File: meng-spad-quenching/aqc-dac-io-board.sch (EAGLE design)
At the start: 13 parts, among them IC5 NC7WZ16P6X, X1 CONN_VREF_CASCODE_IBIAS, X2 CONN_VREF_DIAMOND_IBIAS, X3 CONN_VREF_ONE_SHOT, X4 CONN_PHOTON_COUNTER, X5 CONN_FORCE_QUENCH

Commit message: Added switch cap inverter
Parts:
- added C1, C6, C7: 4u7, rcl:C-EUC0402
- added C14, C16, C27: 2.2u, rcl:C-USC0603
- added C15, C17, C28, C29: 0.1u, rcl:C-USC0603
- added C2, C3, C4, C5: 100n, rcl:C-EUC0402
- added C24: 470n\, rcl:C-USC0603
- added C33: 47u, rcl:C-USC1206
- added IC2: (no value), microbuilder:VREG_SOT23-5
- added IC3: (no value), Kramnik's Library:TPS72301
- added IC4: MAX1680, Kramnik's Library:MAX1680/1
- added LED1: (no value), led:LED3MM
- added R10: 100k, resistor:R-US_R0603
- added R11: 470R, resistor:R-US_R0805
- added R2, R3: 2k2, resistor:R-EU_R0603
- added R21: 64k, resistor:R-US_R0603
- added R22: 36k, resistor:R-US_R0603
- added TP1: TPTP20SQ, testpad:TPTP20SQ
- added X6: USB-MINIB, adafruit:USBMINIB
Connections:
- removed net N$37: IC5.OUT1, IC5.OUT2
- new net +3V3: C14.1, C15.1, IC2.OUT, R10.2
- new net +5V: C16.1, C17.1, C24.1, C33.1, IC2.EN, IC2.IN, R11.1, X6.VBUS
- new net -3V3: C27.1, C28.1, IC3.OUT, R21.1
- new net -5V: C29.1, IC3.EN, IC3.IN
- new net N$11: LED1.A, R11.2
- new net N$14: C7.2, IC4.CAP-
- new net N$15: C7.1, IC4.CAP+
- new net N$19: IC3.FB, R21.2, R22.1
- new net N$2: C3.1, U1.VDD
- new net N$4: IC2.P4, R10.1
- new net N$6: C5.1, U3.VDD
- new net N$7: C4.1, U2.VDD
- new net N$8: R2.2, R3.2
- new net PP_N5V0: C6.1, IC4.OUT
- new net PP_P5V0: ARDUINO_NANO1.5V, C1.1, C2.1, IC4.IN
- net DAC_SCL: now also R2.1
- net DAC_SDA: now also R3.1
- net FORCE_QUENCH_BUF: now also IC5.OUT1, IC5.OUT2
- net GND: now also ARDUINO_NANO1.GND@1, C1.2, C14.2, C15.2, C16.2, C17.2, C2.2, C24.2, C27.2, C28.2, C29.2, C3.2, C33.2, C4.2, C5.2, C6.2, IC2.GND, IC3.GND, IC4.FSEL, IC4.GND, IC4.LV, IC4.SHDN, LED1.C, R22.2, TP1.TP, X6.GND
- net PP_P3V3: now also ARDUINO_NANO1.3V3
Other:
- note added: "+3.3V Linear Regulator"
- note added: "-3.3V Linear Regulator"
- note added: "-5V Switching Converter"
- note added: "Power LED"
- note added: "Scope Ground Clip"
- note added: "USB (Power) Connector"
- note added: "Voltage levels?"
- moved on the sheet: ARDUINO_NANO1, C30, C31, IC5, R1, U1, U2, U3, X1, X2, X3, X4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

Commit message: Started layout, added rescaling opamp and line driver
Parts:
- removed ARDUINO_NANO1: (no value), ArduinoNanoV30:ARDUINO_NANO
- removed C14, C16, C27: 2.2u, rcl:C-USC0603
- removed C15, C17, C28, C29: 0.1u, rcl:C-USC0603
- removed C24: 470n\, rcl:C-USC0603
- removed C33: 47u, rcl:C-USC1206
- removed IC3: (no value), Kramnik's Library:TPS72301
- removed IC5: NC7WZ16P6X, meng:NC7WZ16P6X
- removed LED1: (no value), led:LED3MM
- removed R10: 100k, resistor:R-US_R0603
- removed R11: 470R, resistor:R-US_R0805
- removed R21: 64k, resistor:R-US_R0603
- removed R22: 36k, resistor:R-US_R0603
- removed TP1: TPTP20SQ, testpad:TPTP20SQ
- removed X6: USB-MINIB, adafruit:USBMINIB
- added C8, C9: 100n, rcl:C-EUC0603
- added H1, H2, H3, H4: MOUNT-PAD-ROUND3.2, holes:MOUNT-PAD-ROUND3.2
- added IC1: LT1366, meng:LT1366
- added R4, R7: 10k0, resistor:R-EU_R0603
- added R5: 15k0, resistor:R-EU_R0603
- added R6: 5k11, resistor:R-EU_R0603
- added STM32_NUCLEO: (no value), ArduinoNanoV30:ARDUINO_NANO
- C1, C6, C7: device rcl:C-EUC0402 -> rcl:C-EUC0805
- C2, C3, C30, C31, C4, C5: device rcl:C-EUC0402 -> rcl:C-EUC0603
- IC2: value (none) -> 74LVT126; device microbuilder:VREG_SOT23-5 -> meng:74LVT126
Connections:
- removed net +3V3: C14.1, C15.1, IC2.OUT, R10.2
- removed net +5V: C16.1, C17.1, C24.1, C33.1, IC2.EN, IC2.IN, R11.1, X6.VBUS
- removed net -3V3: C27.1, C28.1, IC3.OUT, R21.1
- removed net -5V: C29.1, IC3.EN, IC3.IN
- removed net LOGIC_QUENCH: IC5.IN1, IC5.IN2
- removed net N$11: LED1.A, R11.2
- removed net N$19: IC3.FB, R21.2, R22.1
- removed net N$4: IC2.P4, R10.1
- new net FORCE_QUENCH_MCU: IC2.1A
- net DAC_SCL: now also STM32_NUCLEO.ADC5/SCL/A5; no longer ARDUINO_NANO1.ADC5/SCL/A5
- net DAC_SDA: now also STM32_NUCLEO.ADC4/SDA/A4; no longer ARDUINO_NANO1.ADC4/SDA/A4
- net FORCE_QUENCH_BUF: now also IC2.1Y; no longer IC5.OUT1, IC5.OUT2
- net GND: now also C8.2, C9.2, H1.MOUNT, H2.MOUNT, H3.MOUNT, H4.MOUNT, IC1B.+IN, IC2.2A, IC2.2OE, IC2.3A, IC2.3OE, IC2.4A, IC2.4OE, R7.1, STM32_NUCLEO.GND@1, STM32_NUCLEO.GND@2; no longer ARDUINO_NANO1.GND@1, ARDUINO_NANO1.GND@2, C14.2, C15.2, C16.2, C17.2, C24.2, C27.2, C28.2, C29.2, C33.2, IC3.GND, IC5.GND, LED1.C, R22.2, TP1.TP, X6.GND
- net N$2: now also R4.2, U1.VOUT; no longer C3.1, U1.VDD
- net N$3: now also IC1B.-IN, R4.1, R5.2; no longer U2.VOUT, X2G1.1
- net N$5: now also IC1B.OUT, R5.1; no longer U1.VOUT
- net N$6: now also IC1A.+IN, U2.VOUT; no longer C5.1, U3.VDD
- net N$7: now also IC1A.OUT, R6.2, X2G1.1; no longer C4.1, U2.VDD
- net N$8: now also IC1A.-IN, R6.1, R7.2; no longer R2.2, R3.2
- net PP_N5V0: now also C8.1, IC1A.V-
- net PP_P3V3: now also C3.1, C4.1, C5.1, IC2.1OE, IC2.VDD, R2.2, R3.2, STM32_NUCLEO.3V3, U1.VDD, U2.VDD, U3.VDD; no longer ARDUINO_NANO1.3V3, IC5.VCC
- net PP_P5V0: now also C9.1, IC1A.V+, STM32_NUCLEO.5V; no longer ARDUINO_NANO1.5V
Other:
- note added: "0V to -5V"
- note added: "0V to 3.3V"
- note added: "0V to 5V"
- note removed: "+3.3V Linear Regulator"
- note removed: "-3.3V Linear Regulator"
- note removed: "-5V Switching Converter"
- note removed: "Power LED"
- note removed: "Scope Ground Clip"
- note removed: "USB (Power) Connector"
- note removed: "Voltage levels?"
- moved on the sheet: C3, C30, C31, C4, C5, R1, R2, R3, U1, U2, U3, X1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

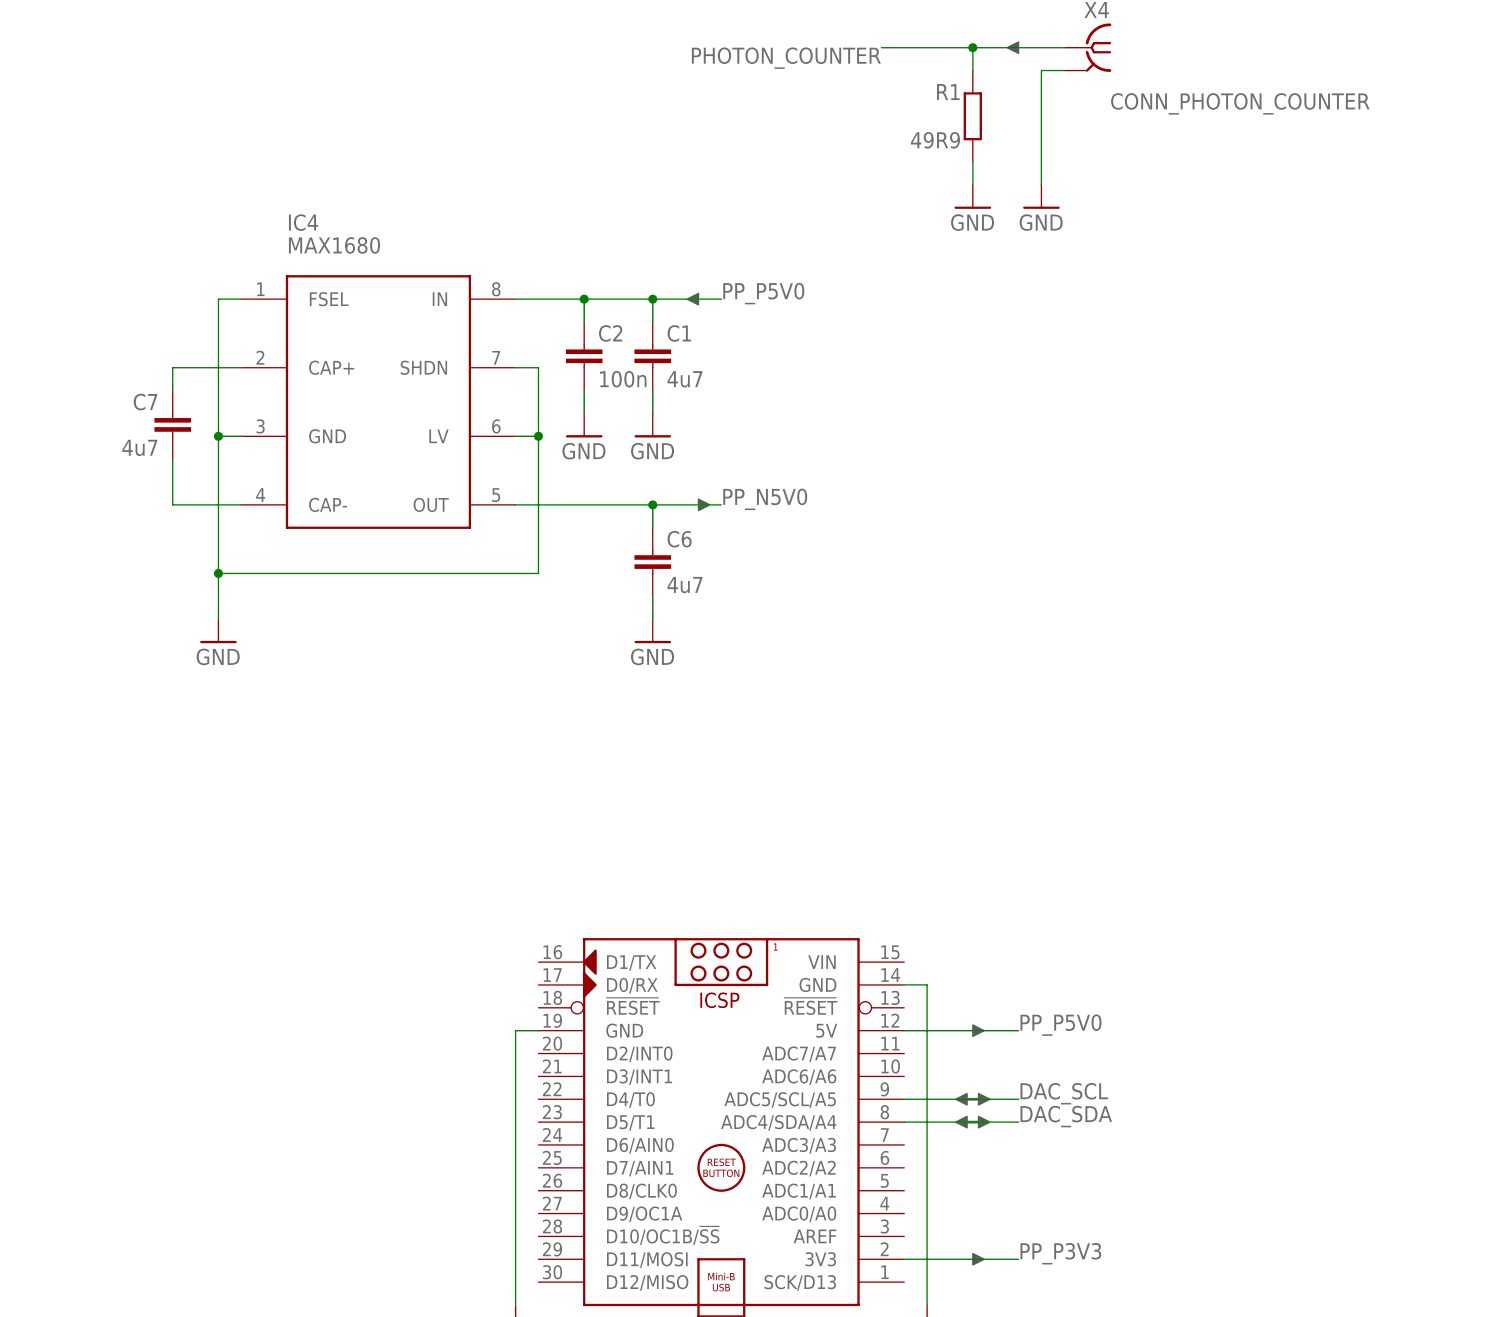
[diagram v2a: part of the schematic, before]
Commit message: Added DIO MCU connections, placed and routed 1st pass
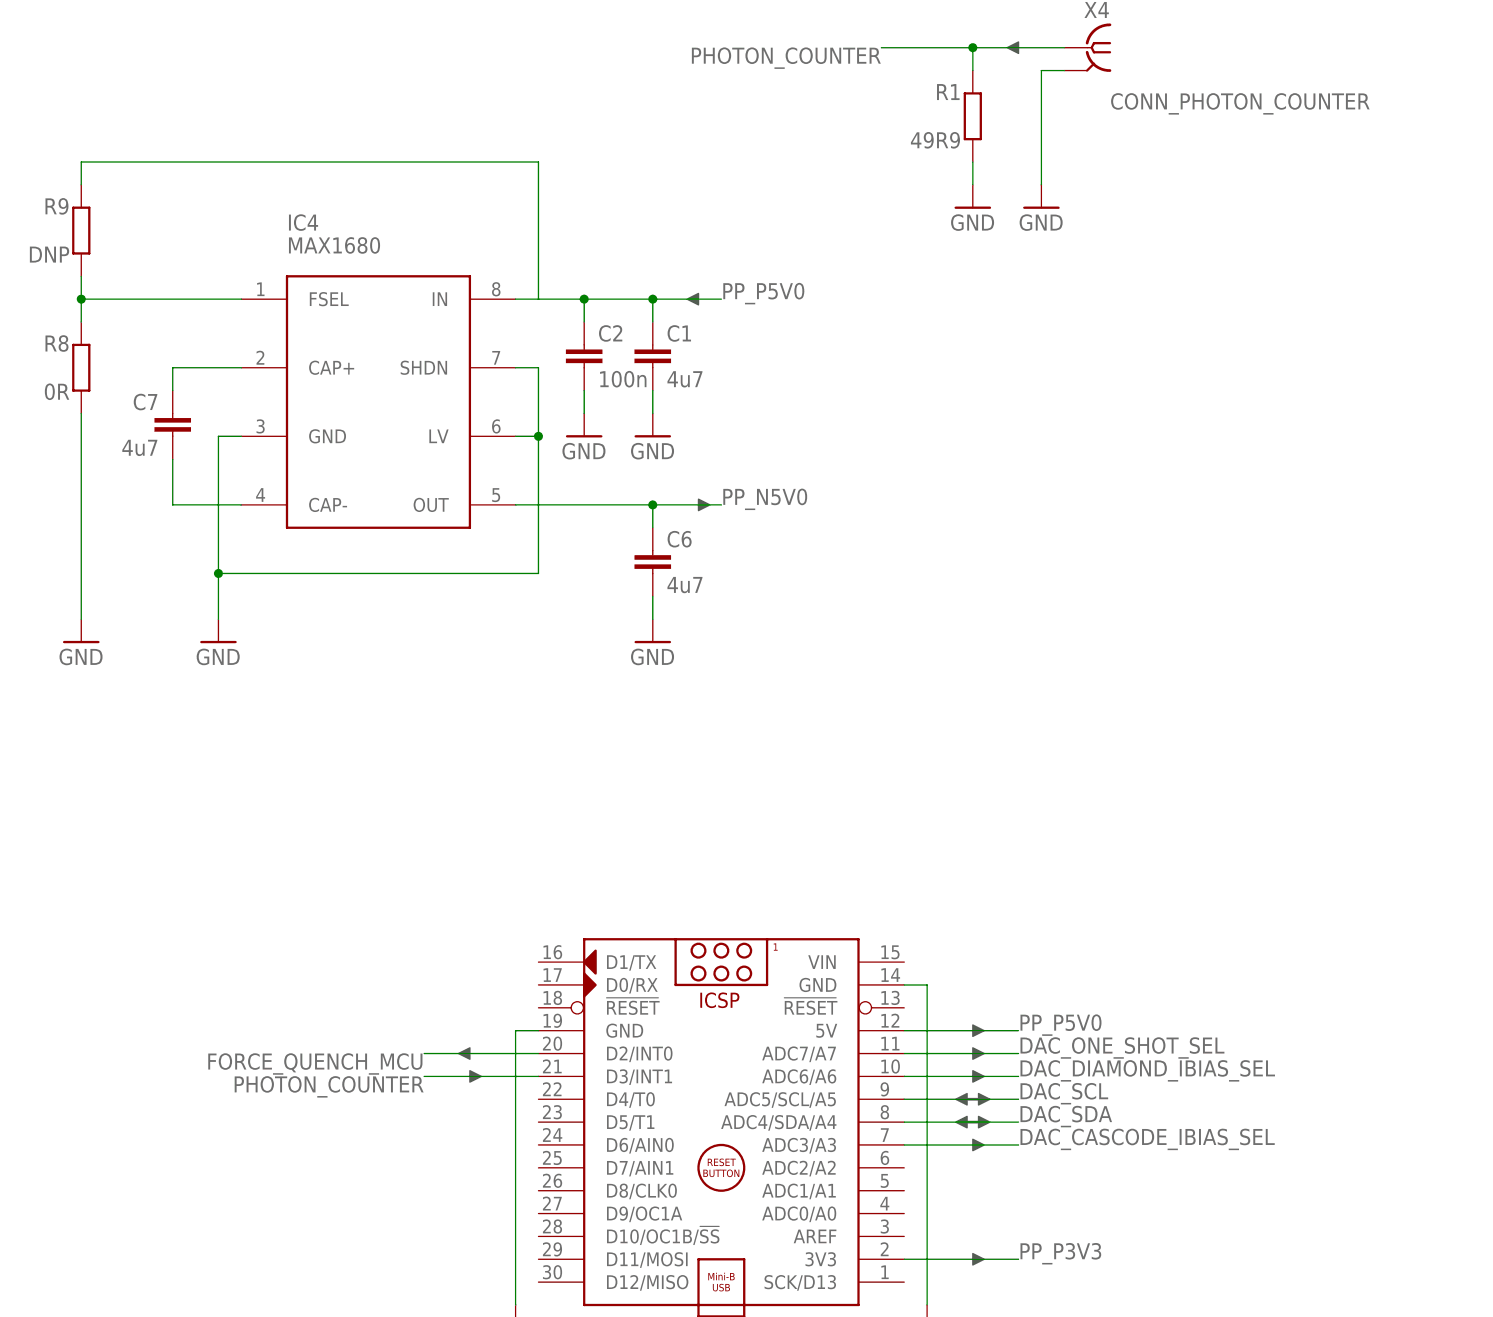
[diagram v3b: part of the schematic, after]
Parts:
- added R8: 0R, resistor:R-EU_R0603
- added R9: DNP, resistor:R-EU_R0603
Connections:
- new net N$4: IC4.FSEL, R8.2, R9.1
- net DAC_CASCODE_IBIAS_SEL: now also STM32_NUCLEO.ADC3/A3
- net DAC_DIAMOND_IBIAS_SEL: now also STM32_NUCLEO.ADC6/A6
- net DAC_ONE_SHOT_SEL: now also STM32_NUCLEO.ADC7/A7
- net FORCE_QUENCH_MCU: now also STM32_NUCLEO.D2/INT0
- net GND: now also R8.1; no longer IC4.FSEL
- net PHOTON_COUNTER: now also STM32_NUCLEO.D3/INT1
- net PP_P5V0: now also R9.2
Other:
- note added: "125kHz"
- note added: "250kHz"
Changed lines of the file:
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@@
 <part name="GND19" library="supply1" deviceset="GND" device=""/>
 <part name="GND10" library="supply1" deviceset="GND" device=""/>
+<part name="R8" library="resistor" deviceset="R-EU_" device="R0603" value="0R"/>
+<part name="R9" library="resistor" deviceset="R-EU_" device="R0603" value="DNP"/>
+<part name="GND20" library="supply1" deviceset="GND" device=""/>
+<part name="U$3" library="Kramnik's Library" deviceset="LEFT_ARROW" device=""/>
+<part name="U$4" library="Kramnik's Library" deviceset="LEFT_ARROW" device=""/>
+<part name="DNP18" library="meng" deviceset="ARROW_1DIR" device=""/>
+<part name="DNP19" library="meng" deviceset="ARROW_1DIR" device=""/>
+<part name="DNP20" library="meng" deviceset="ARROW_1DIR" device=""/>
 </parts>
 <sheets>
@@
 <text x="373.38" y="109.22" size="1.778" layer="98">0V to 5V</text>
 <text x="373.38" y="149.86" size="1.778" layer="98">0V to -5V</text>
+<text x="27.94" y="152.4" size="1.778" layer="98">250kHz</text>
+<text x="27.94" y="160.02" size="1.778" layer="98">125kHz</text>
 </plain>
 <instances>
@@
 <attribute name="VALUE" x="289.56" y="185.42" size="1.778" layer="96"/>
 </instance>
+<instance part="R8" gate="G$1" x="25.4" y="149.86" smashed="yes" rot="R90">
+<attribute name="NAME" x="24.13" y="153.4414" size="1.778" layer="95" rot="R180"/>
+<attribute name="VALUE" x="24.13" y="148.082" size="1.778" layer="96" rot="R180"/>
+</instance>
+<instance part="R9" gate="G$1" x="25.4" y="165.1" smashed="yes" rot="R90">
+<attribute name="NAME" x="24.13" y="168.6814" size="1.778" layer="95" rot="R180"/>
+<attribute name="VALUE" x="24.13" y="163.322" size="1.778" layer="96" rot="R180"/>
+</instance>
+<instance part="GND20" gate="1" x="25.4" y="119.38" smashed="yes">
+<attribute name="VALUE" x="22.86" y="116.84" size="1.778" layer="96"/>
+</instance>
+<instance part="U$3" gate="G$1" x="68.58" y="71.12" rot="R180"/>
+<instance part="U$4" gate="G$1" x="68.58" y="73.66"/>
+<instance part="DNP18" gate="G$1" x="124.46" y="73.66" smashed="yes"/>
+<instance part="DNP19" gate="G$1" x="124.46" y="71.12" smashed="yes"/>
+<instance part="DNP20" gate="G$1" x="124.46" y="63.5" smashed="yes"/>
 </instances>
 <busses>
@@
 </segment>
 <segment>
-<pinref part="IC4" gate="G$1" pin="FSEL"/>
-<wire x1="43.18" y1="157.48" x2="40.64" y2="157.48" width="0.1524" layer="91"/>
-<wire x1="40.64" y1="157.48" x2="40.64" y2="142.24" width="0.1524" layer="91"/>
 <pinref part="IC4" gate="G$1" pin="GND"/>
 <wire x1="40.64" y1="142.24" x2="43.18" y2="142.24" width="0.1524" layer="91"/>
@@
 <wire x1="76.2" y1="127" x2="76.2" y2="142.24" width="0.1524" layer="91"/>
 <junction x="76.2" y="142.24"/>
-<junction x="40.64" y="142.24"/>
 <pinref part="GND17" gate="1" pin="GND"/>
 <wire x1="40.64" y1="121.92" x2="40.64" y2="127" width="0.1524" layer="91"/>
@@
 <junction x="292.1" y="220.98"/>
 </segment>
+<segment>
+<pinref part="R8" gate="G$1" pin="1"/>
+<pinref part="GND20" gate="1" pin="GND"/>
+<wire x1="25.4" y1="144.78" x2="25.4" y2="121.92" width="0.1524" layer="91"/>
+</segment>
 </net>
 <net name="PHOTON_COUNTER" class="0">
@@
 <junction x="124.46" y="185.42"/>
 <label x="114.3" y="185.42" size="1.778" layer="95" rot="R180"/>
+</segment>
+<segment>
+<pinref part="STM32_NUCLEO" gate="G$1" pin="D3/INT1"/>
+<wire x1="76.2" y1="71.12" x2="63.5" y2="71.12" width="0.1524" layer="91"/>
+<label x="63.5" y="71.12" size="1.778" layer="95" rot="R180"/>
 </segment>
 </net>
@@
 <label x="254" y="149.86" size="1.778" layer="95" rot="R180"/>
 </segment>
+<segment>
+<pinref part="STM32_NUCLEO" gate="G$1" pin="ADC3/A3"/>
+<wire x1="116.84" y1="63.5" x2="129.54" y2="63.5" width="0.1524" layer="91"/>
+<label x="129.54" y="63.5" size="1.778" layer="95"/>
+</segment>
 </net>
 <net name="DAC_DIAMOND_IBIAS_SEL" class="0">
@@
 <label x="254" y="109.22" size="1.778" layer="95" rot="R180"/>
 </segment>
+<segment>
+<pinref part="STM32_NUCLEO" gate="G$1" pin="ADC6/A6"/>
+<wire x1="116.84" y1="71.12" x2="129.54" y2="71.12" width="0.1524" layer="91"/>
+<label x="129.54" y="71.12" size="1.778" layer="95"/>
+</segment>
 </net>
 <net name="DAC_ONE_SHOT_SEL" class="0">
@@
 <wire x1="276.86" y1="68.58" x2="254" y2="68.58" width="0.1524" layer="91"/>
 <label x="254" y="68.58" size="1.778" layer="95" rot="R180"/>
+</segment>
+<segment>
+<pinref part="STM32_NUCLEO" gate="G$1" pin="ADC7/A7"/>
+<wire x1="116.84" y1="73.66" x2="129.54" y2="73.66" width="0.1524" layer="91"/>
+<label x="129.54" y="73.66" size="1.778" layer="95"/>
 </segment>
 </net>
@@
 <pinref part="IC2" gate="G$1" pin="1A"/>
 </segment>
+<segment>
+<pinref part="STM32_NUCLEO" gate="G$1" pin="D2/INT0"/>
+<wire x1="76.2" y1="73.66" x2="63.5" y2="73.66" width="0.1524" layer="91"/>
+<label x="63.5" y="73.66" size="1.778" layer="95" rot="R180"/>
+</segment>
 </net>
 <net name="N$14" class="0">
@@
 <segment>
 <pinref part="IC4" gate="G$1" pin="IN"/>
-<wire x1="73.66" y1="157.48" x2="81.28" y2="157.48" width="0.1524" layer="91"/>
+<wire x1="73.66" y1="157.48" x2="76.2" y2="157.48" width="0.1524" layer="91"/>
+<wire x1="76.2" y1="157.48" x2="81.28" y2="157.48" width="0.1524" layer="91"/>
 <wire x1="81.28" y1="157.48" x2="88.9" y2="157.48" width="0.1524" layer="91"/>
 <wire x1="88.9" y1="157.48" x2="88.9" y2="154.94" width="0.1524" layer="91"/>
@@
 <pinref part="C1" gate="G$1" pin="1"/>
 <label x="96.52" y="157.48" size="1.778" layer="95"/>
+<wire x1="76.2" y1="157.48" x2="76.2" y2="172.72" width="0.1524" layer="91"/>
+<pinref part="R9" gate="G$1" pin="2"/>
+<wire x1="76.2" y1="172.72" x2="25.4" y2="172.72" width="0.1524" layer="91"/>
+<wire x1="25.4" y1="172.72" x2="25.4" y2="170.18" width="0.1524" layer="91"/>
 </segment>
 <segment>
@@
 </segment>
 </net>
+<net name="N$4" class="0">
+<segment>
+<pinref part="IC4" gate="G$1" pin="FSEL"/>
+<wire x1="43.18" y1="157.48" x2="25.4" y2="157.48" width="0.1524" layer="91"/>
+<pinref part="R9" gate="G$1" pin="1"/>
+<wire x1="25.4" y1="157.48" x2="25.4" y2="160.02" width="0.1524" layer="91"/>
+<pinref part="R8" gate="G$1" pin="2"/>
+<wire x1="25.4" y1="157.48" x2="25.4" y2="154.94" width="0.1524" layer="91"/>
+<junction x="25.4" y="157.48"/>
+</segment>
+</net>

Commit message: Exported gerbers and BOM
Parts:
- removed C30: 100n, rcl:C-EUC0603
- removed C31: 10n, rcl:C-EUC0603
- added C10: 100n, rcl:C-EUC0603
- added C11: 4u7, rcl:C-EUC0805
- added R10, R11: 2k2, resistor:R-EU_R0603
- added TP1: PP_P5V0, Kramnik's Library:KEYSTONE_5000
- added TP2: GND, Kramnik's Library:KEYSTONE_5000
- added TP3: PP_N5V0, Kramnik's Library:KEYSTONE_5000
- C1, C6: value 4u7 -> 100n; device rcl:C-EUC0805 -> rcl:C-EUC0603
- C4: value 100n -> 10n
- C9: value 100n -> 4u7; device rcl:C-EUC0603 -> rcl:C-EUC0805
- R1: value 49R9 -> 100R
- R2: value 2k2 -> 100R
- R3: value 2k2 -> 15k0
- R4: value 10k0 -> 5k11
- R5: value 15k0 -> 10k0
- R6: value 5k11 -> 10k0
- R7: value 10k0 -> 0R
- R8: value 0R -> DNP
- R9: value DNP -> 0R
- X4: value CONN_PHOTON_COUNTER -> CONN_FORCE_QUENCH
- X5: value CONN_FORCE_QUENCH -> CONN_PHOTON_COUNTER
- renumbered IC4 to IC3
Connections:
- new net N$9: R9.2, STM32_NUCLEO.5V
- net DAC_CASCODE_IBIAS_SEL: now also U3.A0; no longer U1.A0
- net DAC_ONE_SHOT_SEL: now also U1.A0; no longer U3.A0
- net DAC_SCL: now also R10.1; no longer R2.1
- net DAC_SDA: now also R11.1; no longer R3.1
- net FORCE_QUENCH_BUF: now also X4G1.1; no longer X5G1.1
- net GND: now also C10.2, C11.2, C7.2, R2.1, R5.1, TP2.P$1; no longer C30.2, C31.2, C9.2, R8.1
- net N$1: now also U1.VOUT; no longer U3.VOUT
- net N$14: now also C9.2; no longer C7.2
- net N$15: now also C9.1; no longer C7.1
- net N$2: now also R6.2, U3.VOUT; no longer R4.2, U1.VOUT
- net N$3: now also R3.2, R6.1; no longer R4.1, R5.2
- net N$4: now also R7.2, R8.1; no longer R8.2, R9.1
- net N$5: now also R3.1; no longer R5.1
- net N$7: now also R4.2; no longer R6.2
- net N$8: now also R4.1, R5.2; no longer R6.1, R7.2
- net PHOTON_COUNTER: now also R2.2, X5G1.1; no longer X4G1.1
- net PP_N5V0: now also C11.1, C5.1, TP3.P$1; no longer C6.1, C8.1
- net PP_P3V3: now also C10.1, C2.1, C6.1, R10.2, R11.2; no longer C30.1, C31.1, C5.1, R2.2, R3.2
- net PP_P5V0: now also C7.1, C8.1, R8.2, R9.1, TP1.P$1; no longer C2.1, C9.1, R9.2, STM32_NUCLEO.5V
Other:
- moved on the sheet: C1, C2, C3, C4, C5, C6, C7, C8, C9, H1, H2, H3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
